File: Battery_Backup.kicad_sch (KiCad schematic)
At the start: 16 parts, among them J7 Battery, SW3 SW, U4 TP4056, U5 MT3608

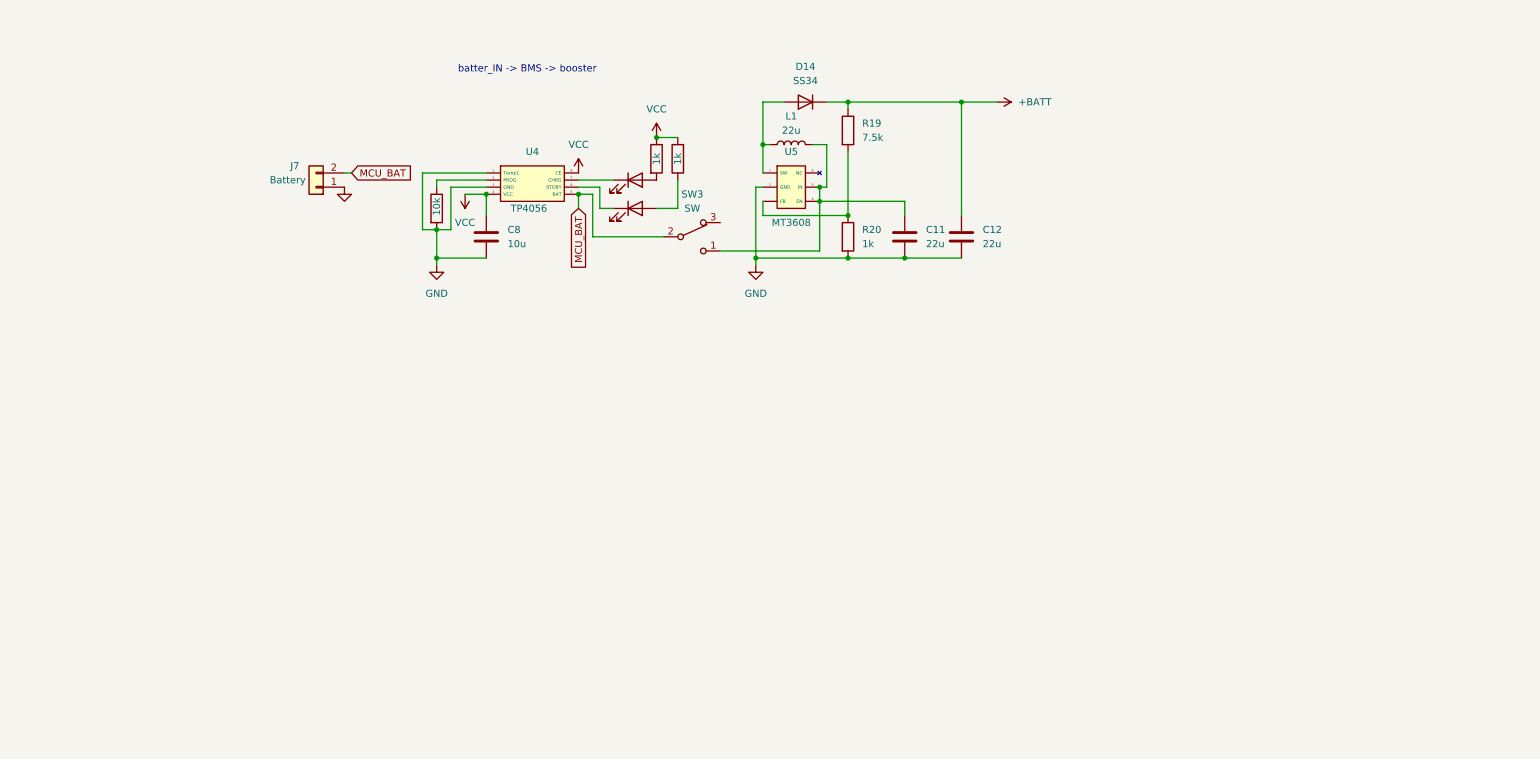
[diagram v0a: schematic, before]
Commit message: Power Section done + added backup lipo
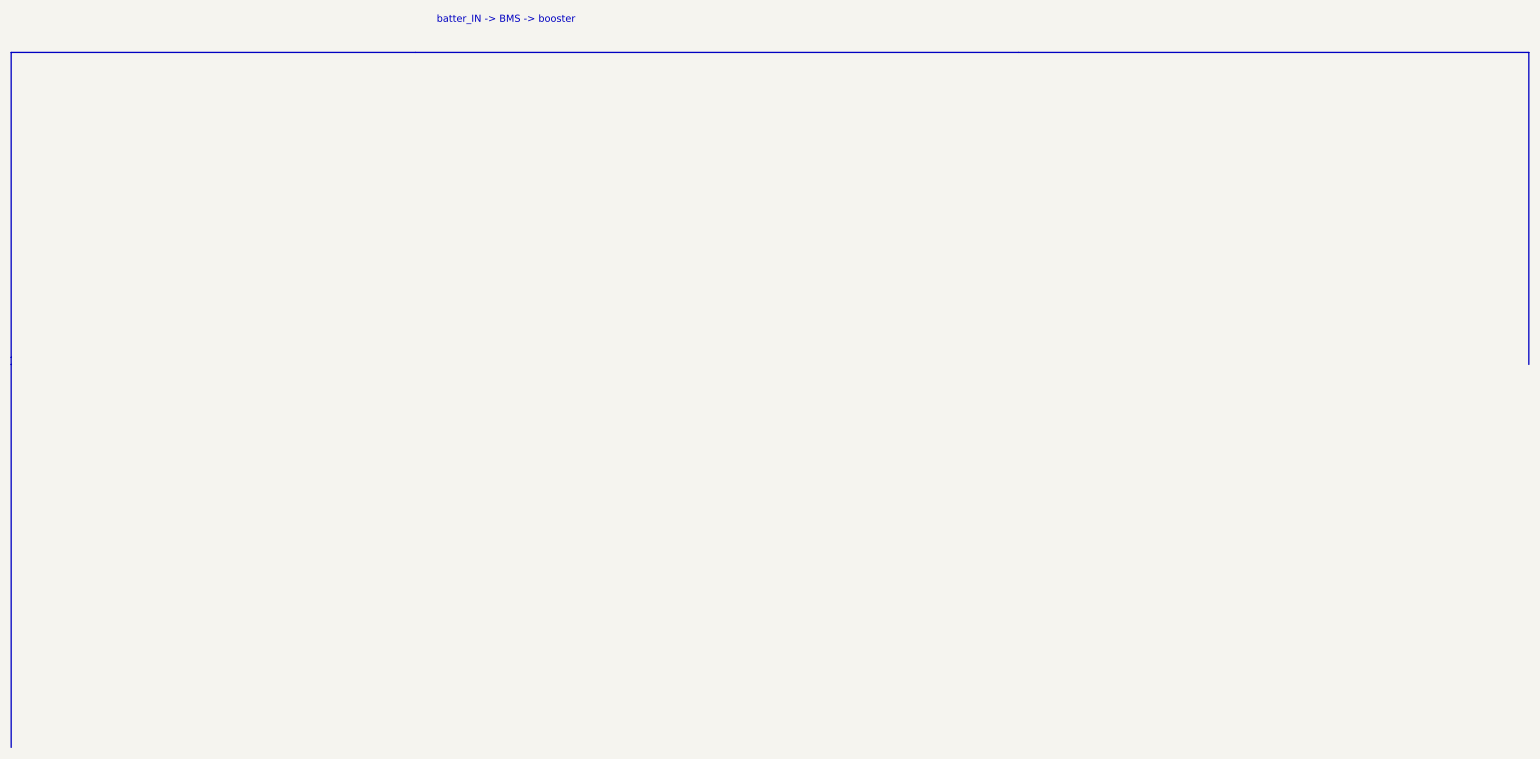
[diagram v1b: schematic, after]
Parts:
- removed C11, C12: 22u, symbol Device:C
- removed C8: 10u, symbol Device:C
- removed D14: SS34, symbol Device:D
- removed D15, D16: LED, symbol Device:LED
- removed J7: Battery, symbol Connector_Generic:Conn_01x02
- removed L1: 22u, symbol Device:L
- removed R16: 10k, symbol Device:R
- removed R17, R18, R20: 1k, symbol Device:R
- removed R19: 7.5k, symbol Device:R
- removed SW3: SW, Button_Switch_SMD:Nidec_Copal_CAS-120A, symbol Switch:SW_Nidec_CAS-120A1
- removed U4: TP4056, symbol Custom:TP4056
- removed U5: MT3608, symbol Custom:MT3608

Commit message: Schematic Completed
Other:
- note removed: "batter_IN -> BMS -> booster"
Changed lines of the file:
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@@
     (stroke (width 0) (type default))
   )
-  (text "batter_IN -> BMS -> booster" (at 88.9 7.62 0)
-    (effects (font (size 1.27 1.27)) (justify left bottom))
-  )
 )
